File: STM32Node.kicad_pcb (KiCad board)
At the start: 2 copper layers, 83 x 83 mm, 12 parts, among them J1 Conn_01x20, J2 Conn_01x18, J3 Conn_Coaxial, J4 Conn_01x03, U1 stm32f103c8t6-module-china, U2 RFM95W-868S2

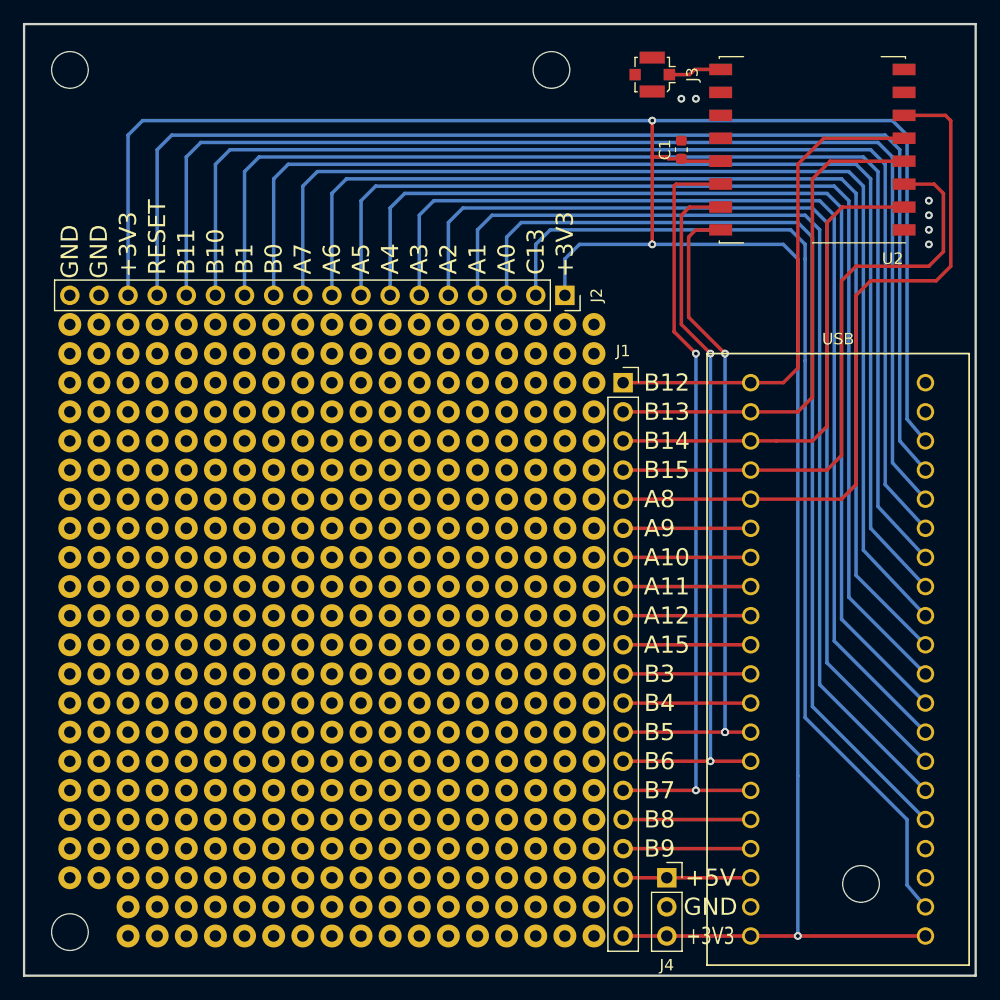
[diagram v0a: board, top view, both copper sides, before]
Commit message: resize board, that it fits into case
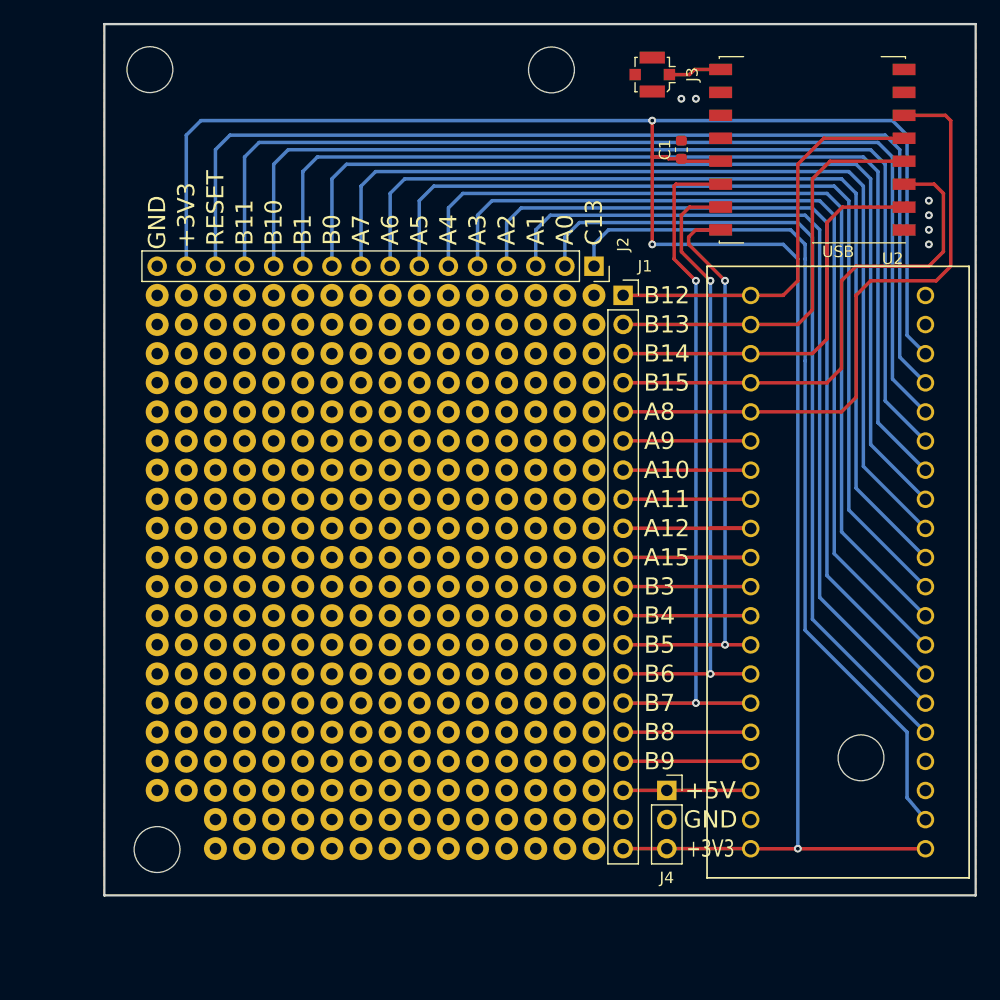
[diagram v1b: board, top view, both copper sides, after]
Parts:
- removed the REF** at (196.8, 104.1)
- added REF**: Lochraster 16x20, Lochraster:Lochraster 16x20, F.Cu at (196.8, 96.5)
- J2: value Conn_01x18 -> Conn_01x16; footprint Connector_PinSocket_2.54mm:PinSocket_1x18_P2.54mm_Vertical -> Connector_PinSocket_2.54mm:PinSocket_1x16_P2.54mm_Vertical
- moved REF** 11.0 mm to (243.0, 114.0)
- moved REF** 10.5 mm to (181.6, 122.0)
- moved J1 7.62 mm to (222.2, 73.7)
- moved J4 7.62 mm to (226.1, 116.8)
- moved U1 7.61 mm to (241.0, 97.8)
- moved REF** 6.98 mm to (181.0, 54.0)
- moved J2 3.59 mm to (219.7, 71.1)
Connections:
- J2 pad 1: +3V3 -> /C13
- J2 pad 10: /A7 -> /B0
- J2 pad 11: /B0 -> /B1
- J2 pad 12: /B1 -> /B10
- J2 pad 13: /B10 -> /B11
- J2 pad 14: /B11 -> /RESET
- J2 pad 15: /RESET -> +3V3
- J2 pad 16: +3V3 -> GND
- J2 pad 2: /C13 -> /A0
- J2 pad 3: /A0 -> /A1
- J2 pad 4: /A1 -> /A2
- J2 pad 5: /A2 -> /A3
- J2 pad 6: /A3 -> /A4
- J2 pad 7: /A4 -> /A5
- J2 pad 8: /A5 -> /A6
- J2 pad 9: /A6 -> /A7
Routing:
- net +3V3: track 237.1 -> 203.0 mm
- net /A4: track 94.3 -> 79.0 mm
- net /C13: track 91.1 -> 75.8 mm
- net /A5: track 95.9 -> 80.7 mm
- net /A2: track 91.0 -> 75.7 mm
- net /A3: track 92.6 -> 77.4 mm
- net /A6: track 97.5 -> 82.3 mm
- net /A1: track 89.3 -> 74.1 mm
- net /A0: track 87.7 -> 72.5 mm
- net /RESET: track 107.3 -> 92.2 mm
- net /B11: track 105.7 -> 90.5 mm
- net /B10: track 104.0 -> 88.9 mm
- net /B1: track 102.4 -> 87.2 mm
- net /B0: track 100.7 -> 85.6 mm
- net /A7: track 99.1 -> 84.0 mm
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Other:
- board size 83 x 83 mm -> 76 x 76 mm
